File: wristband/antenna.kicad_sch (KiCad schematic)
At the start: 4 parts, among them J2 U.FL Hirose U.FL-R-SMT-1

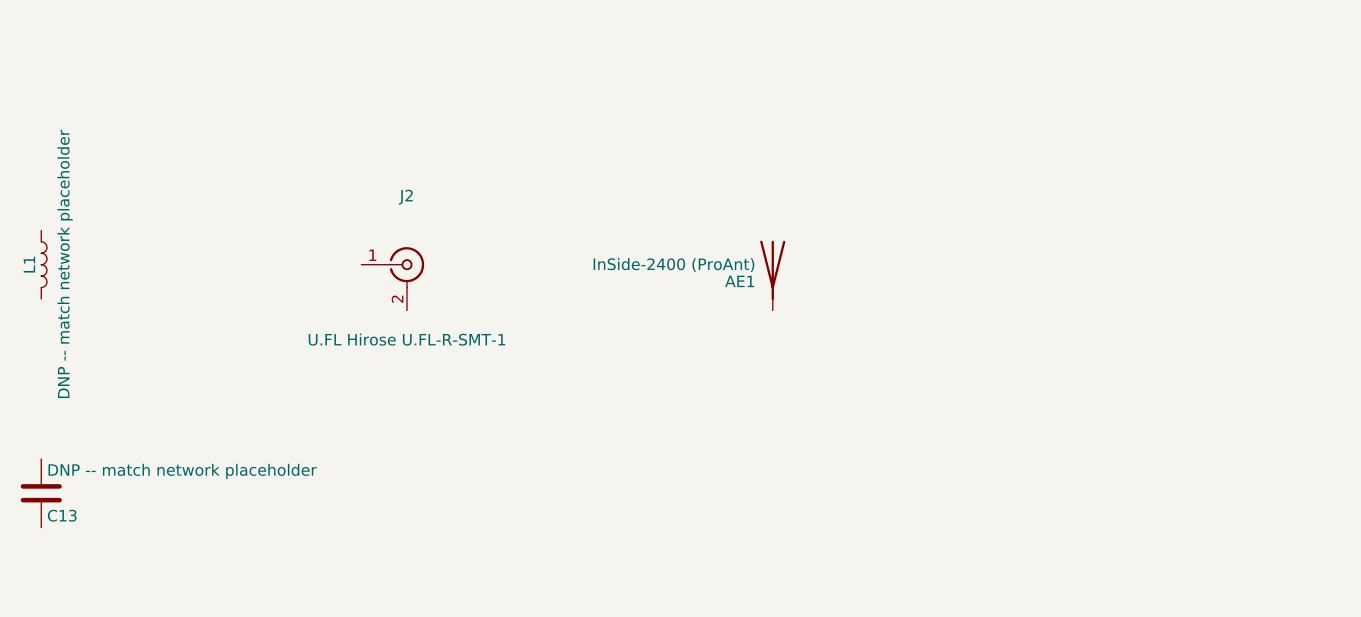
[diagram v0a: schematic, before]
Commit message: Migrate wristband to NINA-B400, wire all sheets, close six design gaps
Replaces the wristband's u-blox NINA-B111 (nRF52832) with a NINA-B400-00B
(Nordic nRF52833, Bluetooth 5.1), then follows through on everything that
change and a full schematic review surfaced.

NINA-B400 migration
- New 55-pin + EGP + EAGP symbol, transcribed from the real NINA-B40 data
  sheet UBX-19049405 R09 Table 6 and cross-checked against Figure 3 for rank
  ordering. Pin numbering validated programmatically (1-55, each exactly once).
- NINA-B4 is pin/mechanically compatible with NINA-B3, NOT NINA-B1, so the
  42-pad NINA111-42 land pattern does not carry over. No official footprint
  exists anywhere -- u-blox's own Eagle library ships only NINA111-42/112-42,
  and neither KiCad's bundled nor upstream RF_Module library has a B3/B4 part.
  NINA-B400-55_PLACEHOLDER is therefore flagged: outline, pad count and rank
  arrangement are confirmed; individual pad X/Y are derived estimates.
  MUST be replaced before fabrication.
- B400 chosen over B401/B406 for its on-module U.FL connector, which let the
  PCB-side U.FL (J2) and the untuned L/C match network (L1/C13) be deleted --
  retiring the project's only open RF-tuning risk.
- No power-design impact: abs-max VCC is 3.9 V on both modules, so the MCP1700
  LDO rationale stands. Budget 12 mA -> 15.5 mA typ; ~70.5 mA with DWM3000
  against 250 mA, ~3.5x headroom (corrects a stale "3.7x" in the docs).
- SWD pin numbers are unchanged (SWDCLK=11, SWDIO=15, RESET_N=19, SWO=8).

Antenna re-verified, part number corrected
- The specified antenna is still pre-approved for NINA-B4 (certification app
  note UBX-20037320 R05 s3.2) but ProAnt was acquired by Abracon and u-blox
  now lists it as PRO-IS-237. Same specs throughout. Order under the Abracon PN.

Six gaps closed
- Y1 + C14/C15: 32.768 kHz LFXO (Epson FC-135, Q13FC13500004). Required for
  lowest sleep current per SIM UBX-19052230 R13 s1.9; XL1/XL2 were floating,
  which Table 6 does not permit eve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
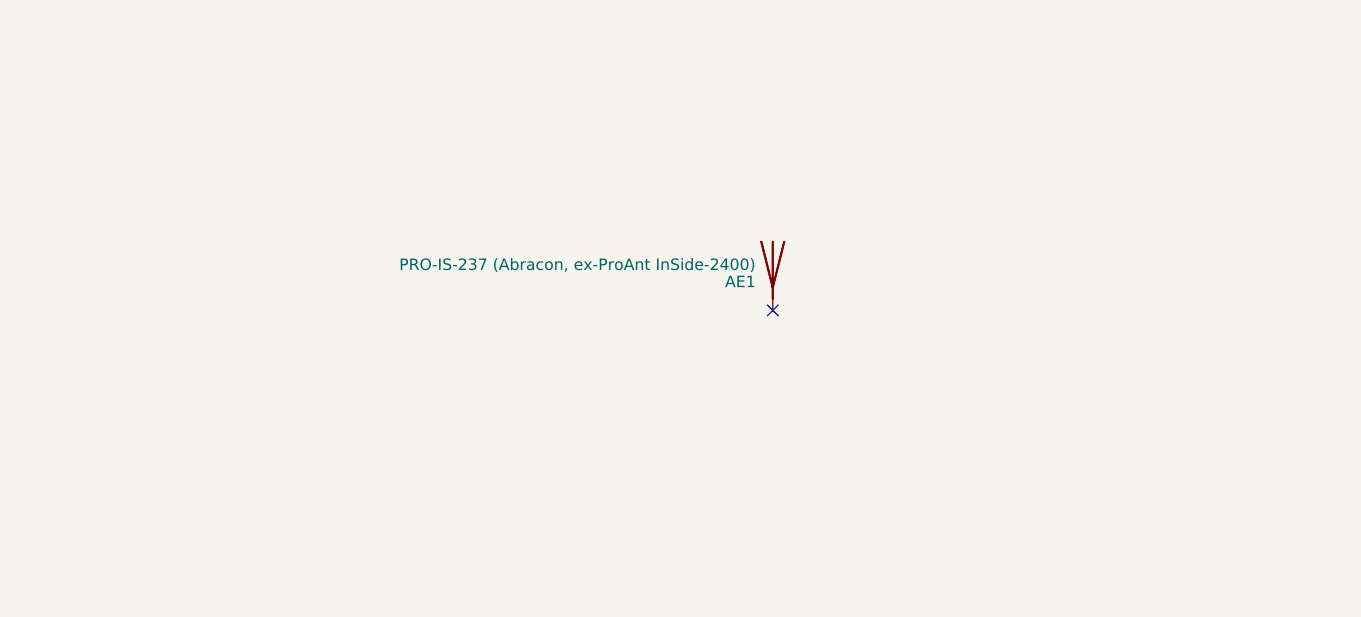
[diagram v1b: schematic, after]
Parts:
- removed C13: DNP -- match network placeholder, Capacitor_SMD:C_0603_1608Metric, symbol Device:C
- removed J2: U.FL Hirose U.FL-R-SMT-1, Connector_Coaxial:U.FL_Hirose_U.FL-R-SMT-1_Vertical, symbol Connector:Conn_Coaxial
- removed L1: DNP -- match network placeholder, Inductor_SMD:L_0603_1608Metric, symbol Device:L
- AE1: value InSide-2400 (ProAnt) -> PRO-IS-237 (Abracon, ex-ProAnt InSide-2400); MPN (none) -> PRO-IS-237; Manufacturer (none) -> Abracon
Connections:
- no-connect marks 0 -> 1
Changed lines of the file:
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@@
 	(title_block
 		(title "Antenna")
-		(comment 1 "Wristband NINA-B111 external antenna (U.FL feed + L/C matching network placeholder) -- placement only, not yet wired")
-	)
-	(symbol
-		(lib_id "Device:L")
-		(at 60.96 76.2 0)
-		(unit 1)
-		(exclude_from_sim no)
-		(in_bom yes)
-		(on_board yes)
-		(dnp no)
-		(property "Reference" "L1"
-			(at 59.69 76.2 90)
-			(effects
-				(font
-					(size 1.27 1.27)
-				)
-			)
-		)
-		(property "Value" "DNP -- match network placeholder"
-			(at 63.5 76.2 90)
-			(effects
-				(font
-					(size 1.27 1.27)
-				)
-			)
-		)
-		(property "Footprint" "Inductor_SMD:L_0603_1608Metric"
-			(at 60.96 76.2 0)
-			(effects
-				(font
-					(size 1.27 1.27)
-				)
-				(hide yes)
-			)
-		)
-		(property "Datasheet" ""
-			(at 60.96 76.2 0)
-			(effects
-				(font
-					(size 1.27 1.27)
-				)
-				(hide yes)
-			)
-		)
-		(pin "1"
-		)
-		(pin "2"
-		)
-		(instances
-			(project "wristband"
-				(path "/b3417696-fb19-4c3e-bd30-28bb2d157bef/70531719-0575-447f-9fe2-78b3cc25b488"
-					(reference "L1")
-					(unit 1)
-				)
-			)
-		)
-	)
-	(symbol
-		(lib_id "Device:C")
-		(at 60.96 101.6 0)
-		(unit 1)
-		(exclude_from_sim no)
-		(in_bom yes)
-		(on_board yes)
-		(dnp no)
-		(property "Reference" "C13"
-			(at 61.595 104.14 0)
-			(effects
-				(font
-					(size 1.27 1.27)
-				)
-				(justify left)
-			)
-		)
-		(property "Value" "DNP -- match network placeholder"
-			(at 61.595 99.06 0)
-			(effects
-				(font
-					(size 1.27 1.27)
-				)
-				(justify left)
-			)
-		)
-		(property "Footprint" "Capacitor_SMD:C_0603_1608Metric"
-			(at 60.96 101.6 0)
-			(effects
-				(font
-					(size 1.27 1.27)
-				)
-				(hide yes)
-			)
-		)
-		(property "Datasheet" ""
-			(at 60.96 101.6 0)
-			(effects
-				(font
-					(size 1.27 1.27)
-				)
-				(hide yes)
-			)
-		)
-		(pin "1"
-		)
-		(pin "2"
-		)
-		(instances
-			(project "wristband"
-				(path "/b3417696-fb19-4c3e-bd30-28bb2d157bef/70531719-0575-447f-9fe2-78b3cc25b488"
-					(reference "C13")
-					(unit 1)
-				)
-			)
-		)
-	)
-	(symbol
-		(lib_id "Connector:Conn_Coaxial")
-		(at 101.6 76.2 0)
-		(unit 1)
-		(exclude_from_sim no)
-		(in_bom yes)
-		(on_board yes)
-		(dnp no)
-		(property "Reference" "J2"
-			(at 101.6 68.58 0)
-			(effects
-				(font
-					(size 1.27 1.27)
-				)
-			)
-		)
-		(property "Value" "U.FL Hirose U.FL-R-SMT-1"
-			(at 101.6 84.582 0)
-			(effects
-				(font
-					(size 1.27 1.27)
-				)
-			)
-		)
-		(property "Footprint" "Connector_Coaxial:U.FL_Hirose_U.FL-R-SMT-1_Vertical"
-			(at 101.6 76.2 0)
-			(effects
-				(font
-					(size 1.27 1.27)
-				)
-				(hide yes)
-			)
-		)
-		(property "Datasheet" ""
-			(at 101.6 76.2 0)
-			(effects
-				(font
-					(size 1.27 1.27)
-				)
-				(hide yes)
-			)
-		)
-		(pin "1"
-		)
-		(pin "2"
-		)
-		(instances
-			(project "wristband"
-				(path "/b3417696-fb19-4c3e-bd30-28bb2d157bef/70531719-0575-447f-9fe2-78b3cc25b488"
-					(reference "J2")
-					(unit 1)
-				)
-			)
-		)
+		(comment 1 "Wristband NINA-B400 external antenna -- plugs into the module's ON-BOARD U.FL connector; no PCB-side U.FL or L/C match network needed")
 	)
 	(symbol
@@
 			)
 		)
-		(property "Value" "InSide-2400 (ProAnt)"
+		(property "Value" "PRO-IS-237 (Abracon, ex-ProAnt InSide-2400)"
 			(at 140.335 76.2 0)
 			(effects
@@
 			)
 		)
+		(property "MPN" "PRO-IS-237"
+			(at 140.335 78.105 0)
+			(effects
+				(font
+					(size 1.27 1.27)
+				)
+				(hide yes)
+			)
+		)
+		(property "Manufacturer" "Abracon"
+			(at 140.335 78.105 0)
+			(effects
+				(font
+					(size 1.27 1.27)
+				)
+				(hide yes)
+			)
+		)
 		(pin "1"
 		)
@@
 		)
 	)
+	(no_connect
+		(at 142.24 81.28)
+	)
 )

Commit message: Make schematics readable: wire stubs, A3 reflow, DWM3000 symbol redraw
Connectivity is unchanged -- verified by diffing the exported netlist against
the previous commit: 34 nets, identical pin membership on every one. This is
presentation only.

The problem was pre-existing, not new. Labels were placed exactly on the pin
endpoint, so label text printed on top of the symbol's own pin name (+3V3
stamped over VCC, UWB_CS over GPIO_1). power_bms had it on U1/U2/Q2 as well;
it only became obvious when the convention was scaled onto a 55-pin part.
Every label now sits at the end of a short wire stub pointing away from the
body, which is the standard KiCad idiom.

DWM3000 symbol redrawn (shared/symbols/)
- The old symbol was a 20mm square carrying pin names like GPIO0/RXOKLED drawn
  vertically along the bottom edge, where they collided with each other inside
  the symbol. No amount of label placement fixes that.
- Now 56 x 41mm, functionally grouped: power/ground/control left, SPI/GPIO
  right, no bottom-edge pins. All 24 pins and every property preserved.
- Checked the blast radius before touching it: bay-station is entirely unwired
  (0 wires, 0 labels on every sheet), so nothing was orphaned. Its cached copy
  is refreshed here and its netlist still exports cleanly at 75 components.

Layout
- radio_mcu and power_bms moved to A3 and reflowed into functional blocks;
  42 symbols repositioned.
- 38 annotations added, carrying the datasheet citations and reasoning that
  previously lived only in the markdown -- LFXO load-cap derivation, the
  ~2.1uA battery-divider tradeoff, why DW01A's GND sits on CELL_N, the LDO
  headroom budget, and the unchanged-from-NINA-B111 SWD pin numbers.

Verification
- Wrote a text-collision checker rather than eyeballing it. It caught two
  classes of bug: duplicated annotations (strip() cleared labels and wires but
  not text, so a second pass layered notes over old ones) and doubled labels on
  stacked same-net pins (USB-C J1 A9/B9, A12/B12;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
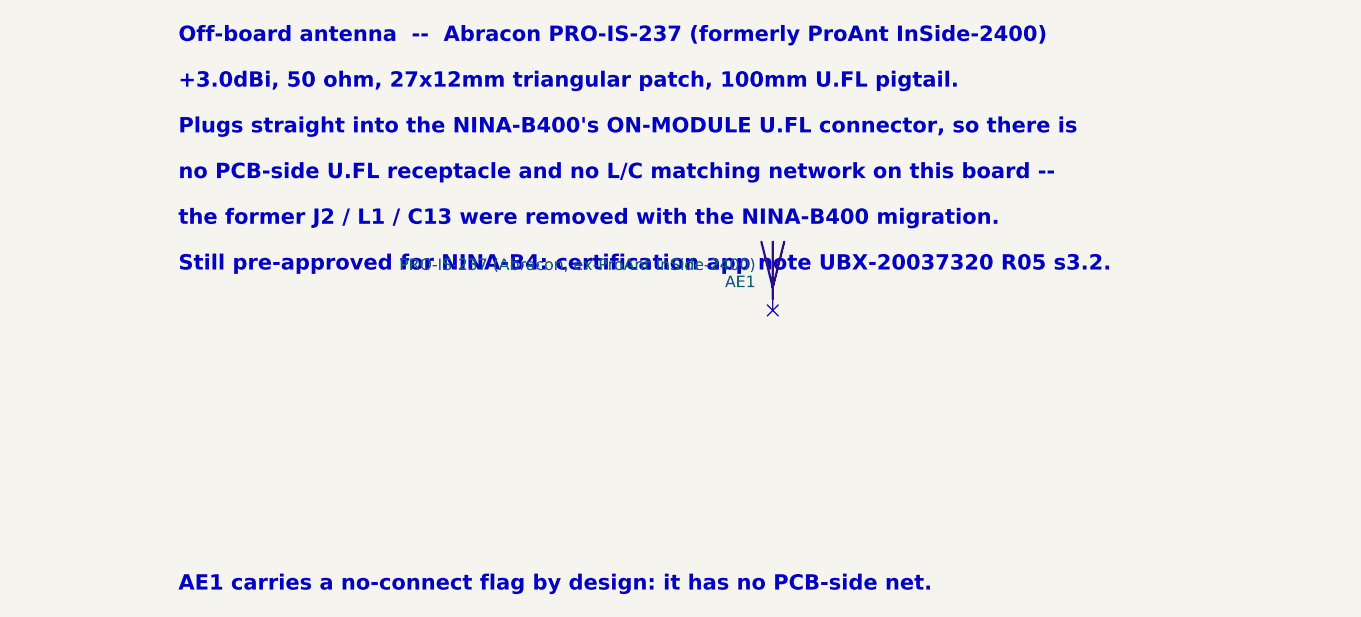
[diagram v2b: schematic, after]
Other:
- note added: "+3.0dBi, 50 ohm, 27x12mm triangular patch, 100mm U.FL pigtail."
- note added: "AE1 carries a no-connect flag by design: it has no PCB-side net."
- note added: "Off-board antenna -- Abracon PRO-IS-237 (formerly ProAnt InSide-2400)"
- note added: "Plugs straight into the NINA-B400's ON-MODULE U.FL connector, so there is"
- note added: "Still pre-approved for NINA-B4: certification app note UBX-20037320 R05 s3.2."
- note added: "no PCB-side U.FL receptacle and no L/C matching network on this board --"
- note added: "the former J2 / L1 / C13 were removed with the NINA-B400 migration."
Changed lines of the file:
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@@
 		(at 142.24 81.28)
 	)
+	(text "Off-board antenna  --  Abracon PRO-IS-237 (formerly ProAnt InSide-2400)"
+		(at 76.2 50.8 0)
+		(effects
+			(font
+				(size 1.7 1.7)
+				(bold yes)
+			)
+			(justify left)
+		)
+	)
+	(text "+3.0dBi, 50 ohm, 27x12mm triangular patch, 100mm U.FL pigtail."
+		(at 76.2 55.88 0)
+		(effects
+			(font
+				(size 1.7 1.7)
+				(bold yes)
+			)
+			(justify left)
+		)
+	)
+	(text "Plugs straight into the NINA-B400's ON-MODULE U.FL connector, so there is"
+		(at 76.2 60.96 0)
+		(effects
+			(font
+				(size 1.7 1.7)
+				(bold yes)
+			)
+			(justify left)
+		)
+	)
+	(text "no PCB-side U.FL receptacle and no L/C matching network on this board --"
+		(at 76.2 66.04 0)
+		(effects
+			(font
+				(size 1.7 1.7)
+				(bold yes)
+			)
+			(justify left)
+		)
+	)
+	(text "the former J2 / L1 / C13 were removed with the NINA-B400 migration."
+		(at 76.2 71.12 0)
+		(effects
+			(font
+				(size 1.7 1.7)
+				(bold yes)
+			)
+			(justify left)
+		)
+	)
+	(text "Still pre-approved for NINA-B4: certification app note UBX-20037320 R05 s3.2."
+		(at 76.2 76.2 0)
+		(effects
+			(font
+				(size 1.7 1.7)
+				(bold yes)
+			)
+			(justify left)
+		)
+	)
+	(text "AE1 carries a no-connect flag by design: it has no PCB-side net."
+		(at 76.2 111.76 0)
+		(effects
+			(font
+				(size 1.7 1.7)
+				(bold yes)
+			)
+			(justify left)
+		)
+	)
 )
